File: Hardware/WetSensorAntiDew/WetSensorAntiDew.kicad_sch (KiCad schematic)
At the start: 30 parts, among them J2 Connector to BME280, J3 4P4C, J5 Connector to power supply, J6 Conn_01x04_Socket, J8 6P6C, Q1 MOSFET N-CH, SW1 SW_Push, U1 AMS1117, U3 STM32F103C6Tx, Y1 Crystal_GND24_Small

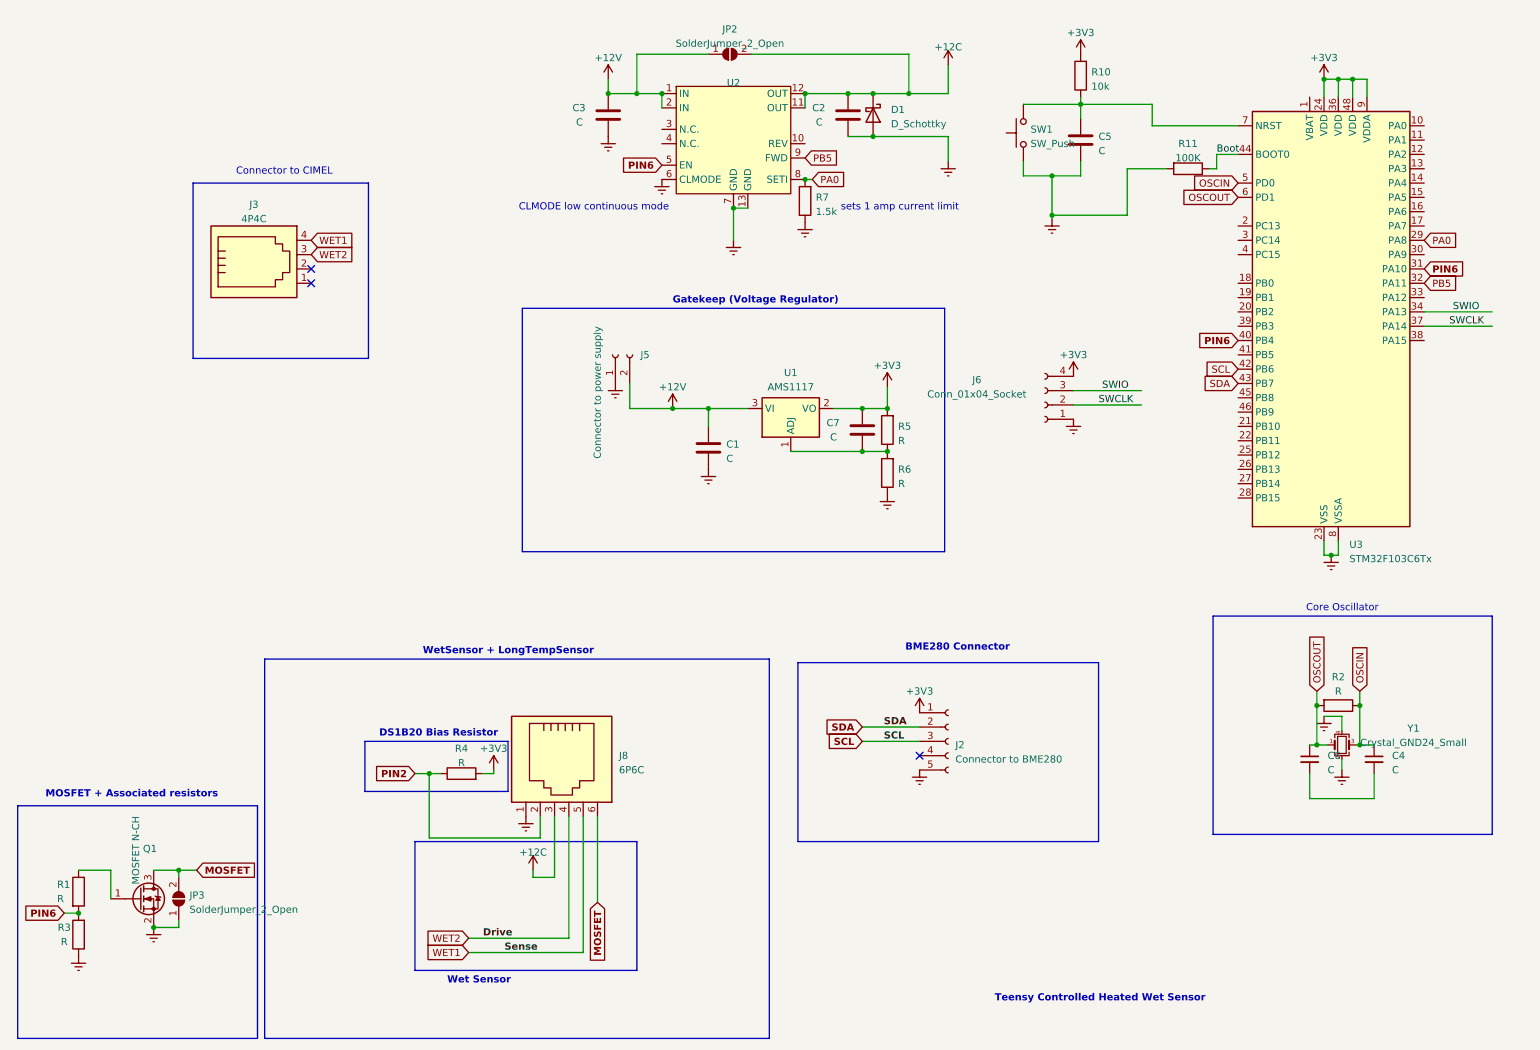
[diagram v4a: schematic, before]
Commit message: Tuned pinouts, corrected N/P switches
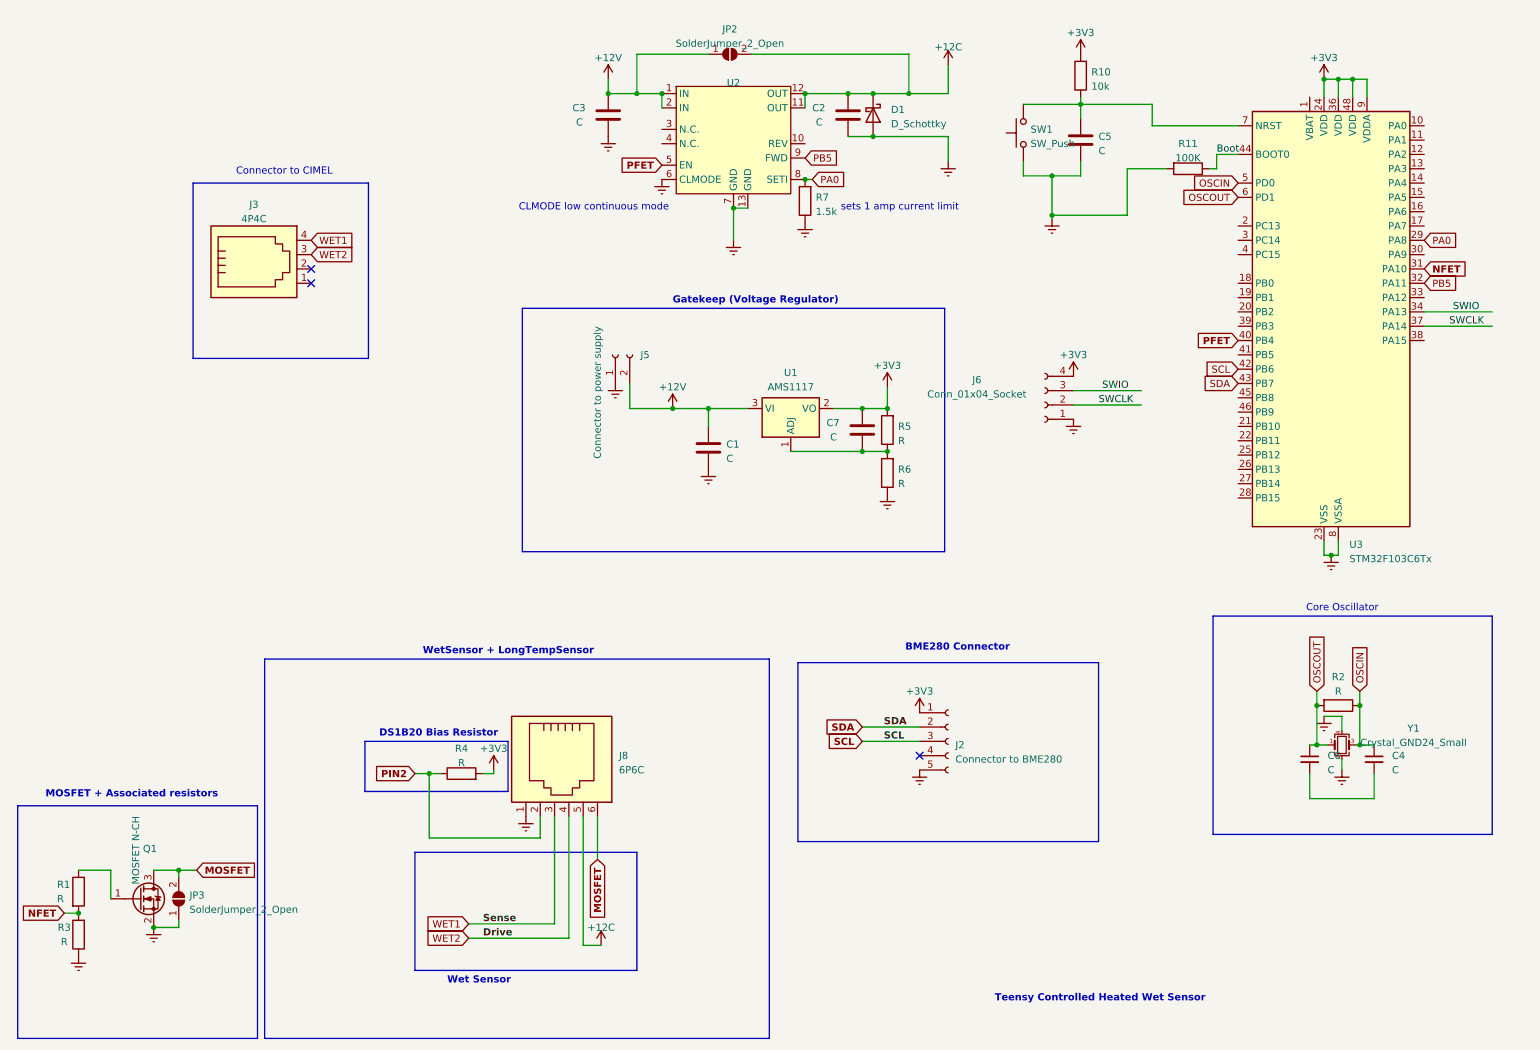
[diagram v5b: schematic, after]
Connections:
- net +12C: now also J8.5; no longer J8.3
- net WET1: now also J8.3; no longer J8.5
- net PIN6 renamed NFET
- net NFET: no longer U2.5 (EN), U3.40 (PB4)
- new net PFET: U2.5 (EN), U3.40 (PB4)
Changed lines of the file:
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@@
-    (stroke (width 0) (type default))
-  )
-  (wire (pts (xy 114.3 157.48) (xy 114.3 181.61))
     (stroke (width 0) (type default))
   )
@@
     (stroke (width 0) (type default))
   )
-  (wire (pts (xy 109.22 168.275) (xy 105.41 168.275))
-    (stroke (width 0) (type default))
-  )
   (wire (pts (xy 243.205 154.305) (xy 254.635 154.305))
     (stroke (width 0) (type default))
@@
     (stroke (width 0) (type default))
   )
+  (wire (pts (xy 93.98 176.53) (xy 109.22 176.53))
+    (stroke (width 0) (type default))
+  )
   (wire (pts (xy 248.285 111.125) (xy 248.285 108.585))
     (stroke (width 0) (type default))
@@
     (stroke (width 0) (type default))
   )
-  (wire (pts (xy 109.22 157.48) (xy 109.22 168.275))
+  (wire (pts (xy 109.22 157.48) (xy 109.22 176.53))
     (stroke (width 0) (type default))
   )
@@
     (stroke (width 0) (type default))
   )
-  (wire (pts (xy 93.98 181.61) (xy 114.3 181.61))
-    (stroke (width 0) (type default))
-  )
   (wire (pts (xy 123.825 22.225) (xy 123.825 29.21))
     (stroke (width 0) (type default))
@@
     (stroke (width 0) (type default))
   )
-  (wire (pts (xy 105.41 168.275) (xy 105.41 167.005))
-    (stroke (width 0) (type default))
-  )
   (wire (pts (xy 248.285 26.67) (xy 248.285 29.845))
     (stroke (width 0) (type default))
@@
     (stroke (width 0) (type default))
   )
-  (wire (pts (xy 116.84 157.48) (xy 116.84 172.72))
+  (wire (pts (xy 116.84 157.48) (xy 116.84 165.1))
     (stroke (width 0) (type default))
   )
@@
     (stroke (width 0) (type default))
   )
+  (wire (pts (xy 117.475 180.34) (xy 114.3 180.34))
+    (stroke (width 0) (type default))
+  )
   (wire (pts (xy 143.51 85.09) (xy 136.525 85.09))
     (stroke (width 0) (type default))
@@
     (stroke (width 0) (type default))
   )
+  (wire (pts (xy 114.3 180.34) (xy 114.3 157.48))
+    (stroke (width 0) (type default))
+  )
   (wire (pts (xy 98.425 149.86) (xy 98.425 149.225))
     (stroke (width 0) (type default))
@@
     (fill (type none))
   )
-  (rectangle (start 84.455 161.925) (end 123.825 184.785)
+  (rectangle (start 84.455 163.83) (end 123.825 184.785)
     (stroke (width 0) (type default))
     (fill (type none))
@@
     (effects (font (size 1.27 1.27) (thickness 0.254) bold) (justify left bottom))
   )
-  (label "Sense" (at 100.33 181.61 0) (fields_autoplaced)
+  (label "Sense" (at 96.52 176.53 0) (fields_autoplaced)
     (effects (font (size 1.27 1.27) bold) (justify left bottom))
   )
@@
     )
   )
-  (global_label "PIN6" (shape input) (at 263.525 60.325 0) (fields_autoplaced)
+  (global_label "NFET" (shape input) (at 263.525 60.325 0) (fields_autoplaced)
     (effects (font (size 1.27 1.27) bold) (justify left))
-    (property "Intersheetrefs" "${INTERSHEET_REFS}" (at 271.274 60.325 0)
+    (property "Intersheetrefs" "${INTERSHEET_REFS}" (at 271.3949 60.325 0)
       (effects (font (size 1.27 1.27)) (justify left) hide)
     )
@@
     )
   )
-  (global_label "PIN6" (shape input) (at 22.225 174.625 180) (fields_autoplaced)
+  (global_label "NFET" (shape input) (at 22.225 174.625 180) (fields_autoplaced)
     (effects (font (size 1.27 1.27) bold) (justify right))
-    (property "Intersheetrefs" "${INTERSHEET_REFS}" (at 14.476 174.625 0)
+    (property "Intersheetrefs" "${INTERSHEET_REFS}" (at 14.3551 174.625 0)
       (effects (font (size 1.27 1.27)) (justify right) hide)
     )
@@
     )
   )
-  (global_label "MOSFET" (shape input) (at 116.84 172.72 270) (fields_autoplaced)
+  (global_label "MOSFET" (shape input) (at 116.84 165.1 270) (fields_autoplaced)
     (effects (font (size 1.27 1.27) bold) (justify right))
-    (property "Intersheetrefs" "${INTERSHEET_REFS}" (at 116.84 183.2508 90)
+    (property "Intersheetrefs" "${INTERSHEET_REFS}" (at 116.84 175.6308 90)
       (effects (font (size 1.27 1.27)) (justify right) hide)
     )
@@
     )
   )
-  (global_label "PIN6" (shape input) (at 230.505 73.025 180) (fields_autoplaced)
+  (global_label "PFET" (shape input) (at 230.505 73.025 180) (fields_autoplaced)
     (effects (font (size 1.27 1.27) bold) (justify right))
-    (property "Intersheetrefs" "${INTERSHEET_REFS}" (at 222.756 73.025 0)
+    (property "Intersheetrefs" "${INTERSHEET_REFS}" (at 222.6956 73.025 0)
       (effects (font (size 1.27 1.27)) (justify right) hide)
     )
@@
     )
   )
-  (global_label "PIN6" (shape input) (at 128.27 41.91 180) (fields_autoplaced)
+  (global_label "PFET" (shape input) (at 128.27 41.91 180) (fields_autoplaced)
     (effects (font (size 1.27 1.27) bold) (justify right))
-    (property "Intersheetrefs" "${INTERSHEET_REFS}" (at 120.521 41.91 0)
+    (property "Intersheetrefs" "${INTERSHEET_REFS}" (at 120.4606 41.91 0)
       (effects (font (size 1.27 1.27)) (justify right) hide)
     )
@@
     )
   )
-  (global_label "WET1" (shape input) (at 93.98 181.61 180) (fields_autoplaced)
+  (global_label "WET1" (shape input) (at 93.98 176.53 180) (fields_autoplaced)
     (effects (font (size 1.27 1.27)) (justify right))
-    (property "Intersheetrefs" "${INTERSHEET_REFS}" (at 86.2967 181.61 0)
+    (property "Intersheetrefs" "${INTERSHEET_REFS}" (at 86.2967 176.53 0)
       (effects (font (size 1.27 1.27)) (justify right) hide)
     )
@@
     )
   )
+  (symbol (lib_id "power:+12C") (at 117.475 180.34 0) (unit 1)
+    (in_bom yes) (on_board yes) (dnp no) (fields_autoplaced)
+    (property "Reference" "#PWR016" (at 117.475 184.15 0)
+      (effects (font (size 1.27 1.27)) hide)
+    )
+    (property "Value" "+12C" (at 117.475 177.165 0)
+      (effects (font (size 1.27 1.27)))
+    )
+    (property "Footprint" "" (at 117.475 180.34 0)
+      (effects (font (size 1.27 1.27)) hide)
+    )
+    (property "Datasheet" "" (at 117.475 180.34 0)
+      (effects (font (size 1.27 1.27)) hide)
+    )
+    (pin "1")
+    (instances
+      (project "WetSensorAntiDew"
+        (path "/4d9ca3a9-89cf-4a0b-a8ab-770e84bd9292"
+          (reference "#PWR016") (unit 1)
+        )
+      )
+    )
+  )
   (symbol (lib_id "Device:R") (at 248.285 137.795 270) (unit 1)
     (in_bom yes) (on_board yes) (dnp no) (fields_autoplaced)
@@
         )
       )
-    )
-  )
-  (symbol (lib_id "power:+12C") (at 105.41 167.005 0) (unit 1)
-    (in_bom yes) (on_board yes) (dnp no) (fields_autoplaced)
-    (property "Reference" "#PWR016" (at 105.41 170.815 0)
-      (effects (font (size 1.27 1.27)) hide)
-    )
-    (property "Value" "+12C" (at 105.41 163.83 0)
-      (effects (font (size 1.27 1.27)))
-    )
-    (property "Footprint" "" (at 105.41 167.005 0)
-      (effects (font (size 1.27 1.27)) hide)
-    )
-    (property "Datasheet" "" (at 105.41 167.005 0)
-      (effects (font (size 1.27 1.27)) hide)
-    )
-    (pin "1")
-    (instances
-      (project "WetSensorAntiDew"
-        (path "/4d9ca3a9-89cf-4a0b-a8ab-770e84bd9292"
-          (reference "#PWR016") (unit 1)
-        )
-      )

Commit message: Final design review pre-fab tuning
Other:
- note added: "BME280 Connector (Gaslight)"
- note added: "Core Oscillator (Luna{Girlboss})"
- note added: "Jumper R6 for fixed AMS1117, DNP R5"
- note added: "Just Truckin' (Load Driver)"
- note added: "SWD PROG"
- note removed: "BME280 Connector"
- note removed: "Core Oscillator"
- moved on the sheet: C1, C2, C3, C7, D1, J2, J3, J5, J8, JP2, JP3, Q1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
